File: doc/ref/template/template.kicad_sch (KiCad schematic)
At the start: 41 parts, among them J1 Conn_02x20_Odd_Even, J10 Conn_01x01, J11 Conn_01x01, J12 Conn_01x01, J13 Conn_01x01, J14 Conn_01x01, J15 Conn_01x01, J16 Conn_01x01, J17 Conn_01x01, J18 Conn_01x01, J19 Conn_01x01, J2 Conn_01x01, J20 Conn_01x01, J21 Conn_01x01, J26 Conn_01x01, J27 Conn_01x01, J28 Conn_01x01, J29 Conn_01x01, J3 Conn_01x01, J30 Conn_01x01, J31 Conn_01x01, J32 Conn_01x01, J33 Conn_01x01, J34 Conn_01x01, J35 Conn_01x01, J36 Conn_01x01, J37 Conn_01x01, J38 Conn_01x01, J39 Conn_01x01, J4 Conn_01x01, J40 Conn_01x01, J41 Conn_01x01, J42 Conn_01x01, J43 Conn_01x01, J44 Conn_01x01, J45 Conn_01x01, J5 Conn_01x01, J6 Conn_01x01, J7 Conn_01x01, J8 Conn_01x01, J9 Conn_01x01

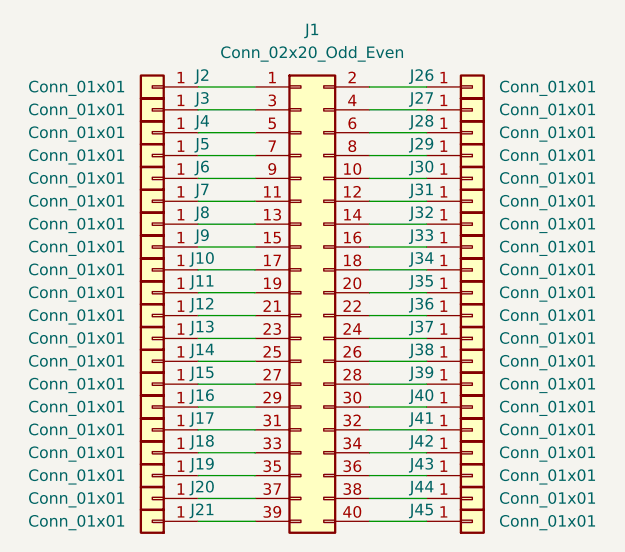
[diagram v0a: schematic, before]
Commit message: removed unused pins on template schematic
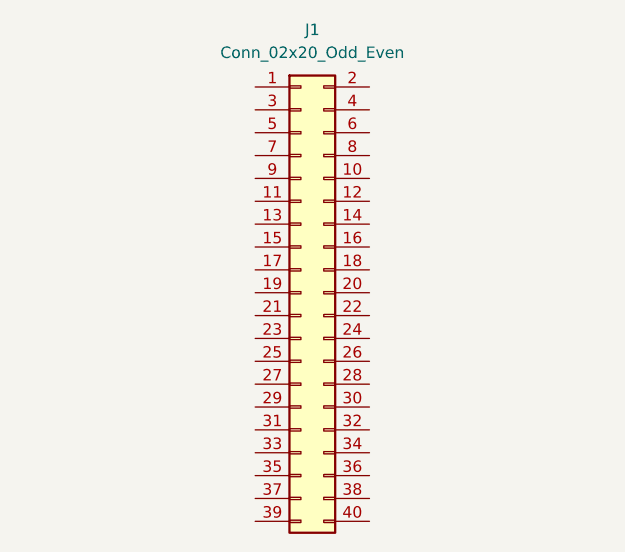
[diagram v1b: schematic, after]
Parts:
- removed J10, J11, J12, J13, J14, J15, J16, J17, J18, J19, J2, J20, J21, J26, J27, J28, J29, J3, J30, J31, J32, J33, J34, J35, J36, J37, J38, J39, J4, J40, J41, J42, J43, J44, J45, J5, J6, J7, J8, J9: Conn_01x01, symbol Connector_Generic:Conn_01x01
